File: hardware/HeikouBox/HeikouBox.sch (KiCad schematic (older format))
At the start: 4 parts

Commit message: More tidy up, move vias
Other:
- moved on the sheet: MH1, MH2, MH3, MH4

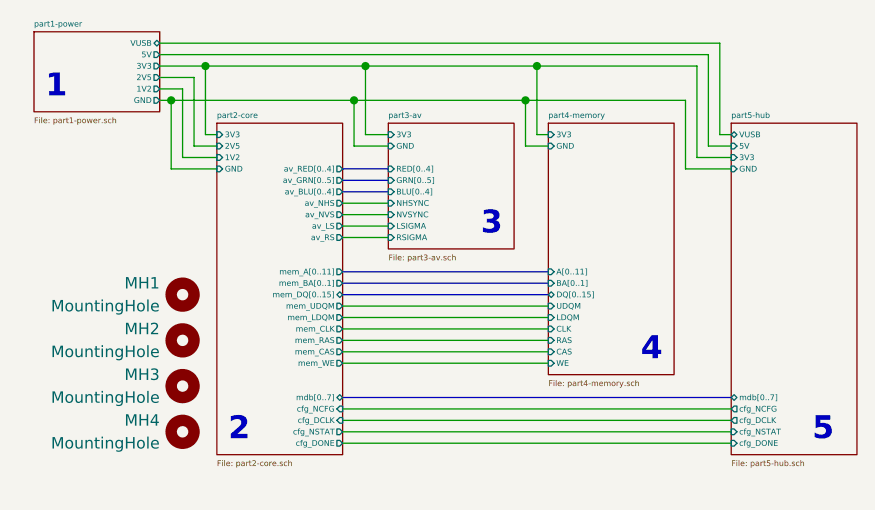
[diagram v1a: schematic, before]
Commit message: Connect UART correctly, remove unused mdb connection & mdb terminology
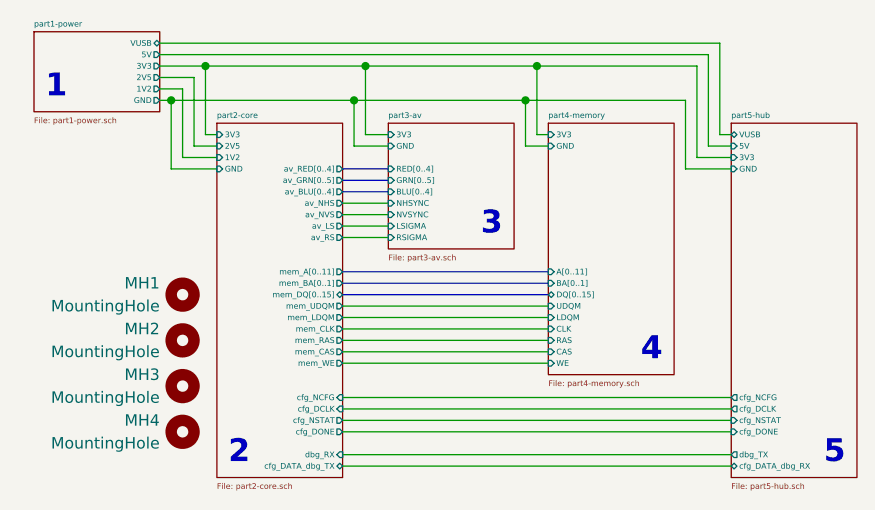
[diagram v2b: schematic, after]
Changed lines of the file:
@@
 Comment4 ""
 $EndDescr
-Wire Bus Line
-	1900 2150 3600 2150
 $Comp
 L Mechanical:MountingHole MH1
@@
 Text Notes 600  850  0    100  ~ 20
 1
-Text Notes 1400 2350 0    100  ~ 20
+Text Notes 1400 2450 0    100  ~ 20
 2
 Wire Bus Line
@@
 	1900 2000 2800 2000
 Wire Wire Line
-	1900 2200 3600 2200
-Wire Wire Line
-	3600 2250 1900 2250
+	1900 2150 3600 2150
+Wire Wire Line
+	3600 2200 1900 2200
+Wire Wire Line
+	1900 2250 3600 2250
 Wire Wire Line
 	1900 2300 3600 2300
-Wire Wire Line
-	1900 2350 3600 2350
 $Sheet
 S 2100 950  550  550
@@
 Wire Wire Line
 	2800 1050 2700 1050
-Text Notes 4050 2350 2    100  ~ 20
+Text Notes 4100 2450 2    100  ~ 20
 5
 Text Notes 3300 2000 2    100  ~ 20
@@
 	1100 650  3500 650
 $Sheet
-S 3600 950  550  1450
+S 3600 950  550  1550
 U 646E3FCF
 F0 "part5-hub" 25
@@
 F3 "GND" I L 3600 1150 25
 F4 "3V3" I L 3600 1100 25
-F5 "cfg_NCFG" O L 3600 2200 25
-F6 "cfg_NSTAT" I L 3600 2300 25
-F7 "cfg_DCLK" O L 3600 2250 25
-F8 "mdb[0..7]" B L 3600 2150 25
-F9 "cfg_DONE" I L 3600 2350 25
-F10 "5V" I L 3600 1050 25
+F5 "cfg_NCFG" O L 3600 2150 25
+F6 "cfg_NSTAT" I L 3600 2250 25
+F7 "cfg_DCLK" O L 3600 2200 25
+F8 "cfg_DONE" I L 3600 2300 25
+F9 "5V" I L 3600 1050 25
+F10 "dbg_TX" O L 3600 2400 25
+F11 "cfg_DATA_dbg_RX" B L 3600 2450 25
 $EndSheet
 Wire Wire Line
@@
 $EndSheet
 $Sheet
-S 1350 950  550  1450
+S 1350 950  550  1550
 U 71351D1D
 F0 "part2-core" 25
@@
 F5 "av_LS" O R 1900 1400 25
 F6 "av_RS" O R 1900 1450 25
-F7 "cfg_DCLK" I R 1900 2250 25
-F8 "cfg_NCFG" I R 1900 2200 25
-F9 "cfg_NSTAT" O R 1900 2300 25
+F7 "cfg_DCLK" I R 1900 2200 25
+F8 "cfg_NCFG" I R 1900 2150 25
+F9 "cfg_NSTAT" O R 1900 2250 25
 F10 "av_NHS" O R 1900 1300 25
 F11 "av_NVS" O R 1900 1350 25
@@
 F13 "mem_LDQM" O R 1900 1800 25
 F14 "mem_CLK" O R 1900 1850 25
-F15 "cfg_DONE" O R 1900 2350 25
+F15 "cfg_DONE" O R 1900 2300 25
 F16 "mem_WE" O R 1900 2000 25
 F17 "mem_CAS" O R 1900 1950 25
@@
 F21 "av_GRN[0..5]" O R 1900 1200 25
 F22 "av_RED[0..4]" O R 1900 1150 25
-F23 "mdb[0..7]" B R 1900 2150 25
-F24 "mem_DQ[0..15]" B R 1900 1700 25
-F25 "mem_A[0..11]" O R 1900 1600 25
-F26 "mem_BA[0..1]" O R 1900 1650 25
-$EndSheet
+F23 "mem_DQ[0..15]" B R 1900 1700 25
+F24 "mem_A[0..11]" O R 1900 1600 25
+F25 "mem_BA[0..1]" O R 1900 1650 25
+F26 "dbg_RX" I R 1900 2400 25
+F27 "cfg_DATA_dbg_TX" B R 1900 2450 25
+$EndSheet
+Wire Wire Line
+	1900 2400 3600 2400
+Wire Wire Line
+	3600 2450 1900 2450
 $EndSCHEMATC
